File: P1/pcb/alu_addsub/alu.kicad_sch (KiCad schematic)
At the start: 33 parts, among them J1 650473-5, U1 74HC86, U10 74LS08, U13 74LS541, U14 74HC86, U15 74HC86, U2 74LS08, U29 74HC238, U3 74LS32, U30 74LS32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

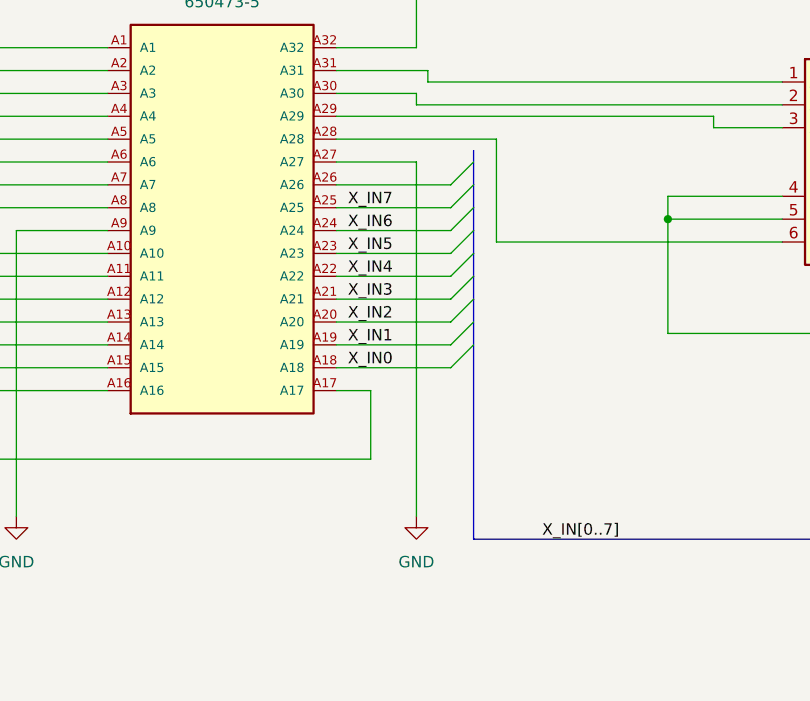
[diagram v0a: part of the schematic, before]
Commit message: Removed unneeded backup files
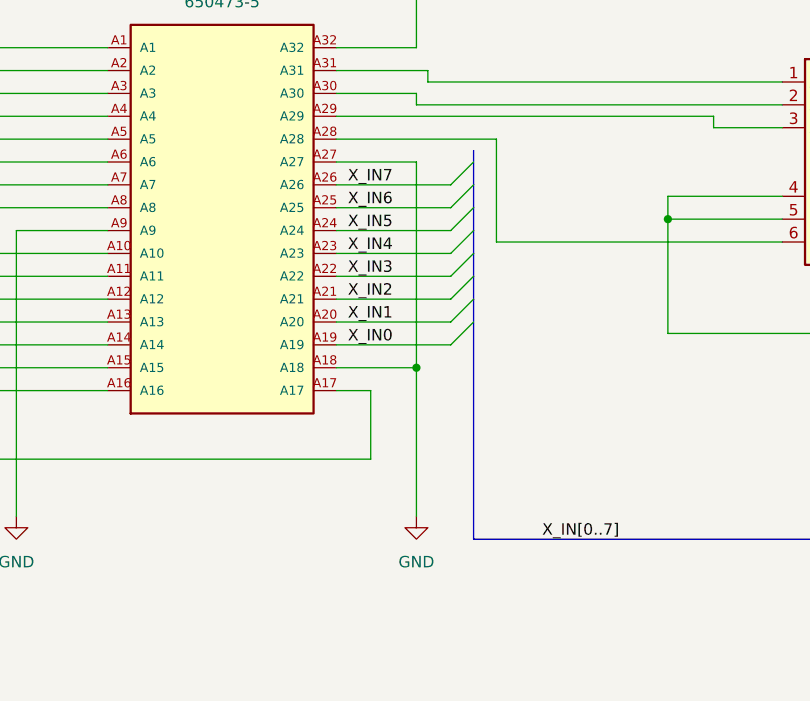
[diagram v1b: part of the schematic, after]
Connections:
- net GND: now also J1.A18
- net X_IN0: now also J1.A19; no longer J1.A18
- net X_IN1: now also J1.A20; no longer J1.A19
- net X_IN2: now also J1.A21; no longer J1.A20
- net X_IN3: now also J1.A22; no longer J1.A21
- net X_IN4: now also J1.A23; no longer J1.A22
- net X_IN5: now also J1.A24; no longer J1.A23
- net X_IN6: now also J1.A25; no longer J1.A24
- net X_IN7: now also J1.A26; no longer J1.A25
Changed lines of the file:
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@@
 	)
 	(junction
+		(at 119.38 73.66)
+		(diameter 0)
+		(color 0 0 0 0)
+	)
+	(junction
 		(at 416.56 530.86)
 		(diameter 0)
@@
 	)
 	(bus_entry
-		(at 123.19 73.66)
-		(size 2.54 -2.54)
-		(stroke
-			(width 0)
-			(type default)
-		)
-	)
-	(bus_entry
 		(at 702.31 118.11)
 		(size 2.54 2.54)
@@
 	(wire
 		(pts
+			(xy 119.38 73.66) (xy 119.38 90.17)
+		)
+		(stroke
+			(width 0)
+			(type default)
+		)
+	)
+	(wire
+		(pts
 			(xy 411.48 312.42) (xy 416.56 312.42)
 		)
@@
 	(wire
 		(pts
+			(xy 110.49 73.66) (xy 119.38 73.66)
+		)
+		(stroke
+			(width 0)
+			(type default)
+		)
+	)
+	(wire
+		(pts
 			(xy 34.29 261.62) (xy 34.29 269.24)
 		)
@@
 		)
 	)
-	(bus
-		(pts
-			(xy 125.73 68.58) (xy 125.73 71.12)
-		)
-		(stroke
-			(width 0)
-			(type default)
-		)
-	)
 	(wire
 		(pts
@@
 		)
 	)
-	(wire
-		(pts
-			(xy 110.49 73.66) (xy 123.19 73.66)
-		)
-		(stroke
-			(width 0)
-			(type default)
-		)
-	)
 	(bus
 		(pts
@@
 	(wire
 		(pts
-			(xy 119.38 50.8) (xy 119.38 90.17)
+			(xy 119.38 50.8) (xy 119.38 73.66)
 		)
 		(stroke
@@
 	(bus
 		(pts
-			(xy 125.73 71.12) (xy 125.73 92.71)
+			(xy 125.73 68.58) (xy 125.73 92.71)
 		)
 		(stroke
@@
 		)
 	)
-	(label "X_IN6"
-		(at 111.76 58.42 0)
-		(fields_autoplaced yes)
-		(effects
-			(font
-				(size 1.27 1.27)
-			)
-			(justify left bottom)
-		)
-	)
 	(label "X_IN4"
 		(at 764.54 135.89 0)
@@
 		)
 	)
-	(label "X_IN7"
-		(at 111.76 55.88 0)
-		(fields_autoplaced yes)
-		(effects
-			(font
-				(size 1.27 1.27)
-			)
-			(justify left bottom)
-		)
-	)
 	(label "RESULT1"
 		(at 707.39 120.65 0)
@@
 		)
 	)
-	(label "X_IN0"
-		(at 111.76 73.66 0)
+	(label "Y_OUT4"
+		(at 213.36 246.38 0)
 		(fields_autoplaced yes)
 		(effects
@@
 		)
 	)
-	(label "Y_OUT4"
-		(at 213.36 246.38 0)
+	(label "X_IN2"
+		(at 111.76 66.04 0)
 		(fields_autoplaced yes)
 		(effects
@@
 		)
 	)
+	(label "X_IN4"
+		(at 111.76 60.96 0)
+		(fields_autoplaced yes)
+		(effects
+			(font
+				(size 1.27 1.27)
+			)
+			(justify left bottom)
+		)
+	)
 	(label "Y_OUT7"
 		(at 213.36 289.56 0)
@@
 		)
 	)
+	(label "X_IN7"
+		(at 111.76 53.34 0)
+		(fields_autoplaced yes)
+		(effects
+			(font
+				(size 1.27 1.27)
+			)
+			(justify left bottom)
+		)
+	)
 	(label "RESULT4"
 		(at 662.94 430.53 0)
@@
 		)
 	)
-	(label "X_IN5"
-		(at 111.76 60.96 0)
-		(fields_autoplaced yes)
-		(effects
-			(font
-				(size 1.27 1.27)
-			)
-			(justify left bottom)
-		)
-	)
 	(label "X_IN3"
 		(at 764.54 130.81 0)
@@
 		)
 	)
-	(label "X_IN4"
-		(at 111.76 63.5 0)
+	(label "Y_OUT2"
+		(at 44.45 66.04 0)
 		(fields_autoplaced yes)
 		(effects
@@
 		)
 	)
-	(label "Y_OUT2"
-		(at 44.45 66.04 0)
+	(label "X_OUT1"
+		(at 83.82 185.42 0)
 		(fields_autoplaced yes)
 		(effects
@@
 		)
 	)
-	(label "X_OUT1"
-		(at 83.82 185.42 0)
+	(label "X_IN6"
+		(at 111.76 55.88 0)
 		(fields_autoplaced yes)
 		(effects
@@
 		)
 	)
-	(label "X_IN3"
-		(at 111.76 66.04 0)
-		(fields_autoplaced yes)
-		(effects
-			(font
-				(size 1.27 1.27)
-			)
-			(justify left bottom)
-		)
-	)
 	(label "X_OUT7"
 		(at 83.82 170.18 0)
@@
 		)
 	)
-	(label "X_IN1"
-		(at 111.76 71.12 0)
-		(fields_autoplaced yes)
-		(effects
-			(font
-				(size 1.27 1.27)
-			)
-			(justify left bottom)
-		)
-	)
 	(label "X_OUT7"
 		(at 381 567.69 0)
@@
 		)
 	)
-	(label "X_IN2"
-		(at 111.76 68.58 0)
-		(fields_autoplaced yes)
-		(effects
-			(font
-				(size 1.27 1.27)
-			)
-			(justify left bottom)
-		)
-	)
 	(label "T0"
 		(at 252.73 186.69 0)
@@
 		)
 	)
+	(label "X_IN1"
+		(at 111.76 68.58 0)
+		(fields_autoplaced yes)
+		(effects
+			(font
+				(size 1.27 1.27)
+			)
+			(justify left bottom)
+		)
+	)
 	(label "RESULT6"
 		(at 664.21 533.4 0)
@@
 		)
 	)
+	(label "X_IN3"
+		(at 111.76 63.5 0)
+		(fields_autoplaced yes)
+		(effects
+			(font
+				(size 1.27 1.27)
+			)
+			(justify left bottom)
+		)
+	)
 	(label "X_OUT6"
 		(at 83.82 172.72 0)
@@
 		)
 	)
+	(label "X_IN5"
+		(at 111.76 58.42 0)
+		(fields_autoplaced yes)
+		(effects
+			(font
+				(size 1.27 1.27)
+			)
+			(justify left bottom)
+		)
+	)
 	(label "RESULT7"
 		(at 664.21 574.04 0)
 		(fields_autoplaced yes)
 		(effects
+			(font
+				(size 1.27 1.27)
+			)
+			(justify left bottom)
+		)
+	)
+	(label "X_IN0"
+		(at 111.76 71.12 0)
+		(fields_autoplaced yes)
+		(effects
